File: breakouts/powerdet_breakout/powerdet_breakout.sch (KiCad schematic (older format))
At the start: 22 parts

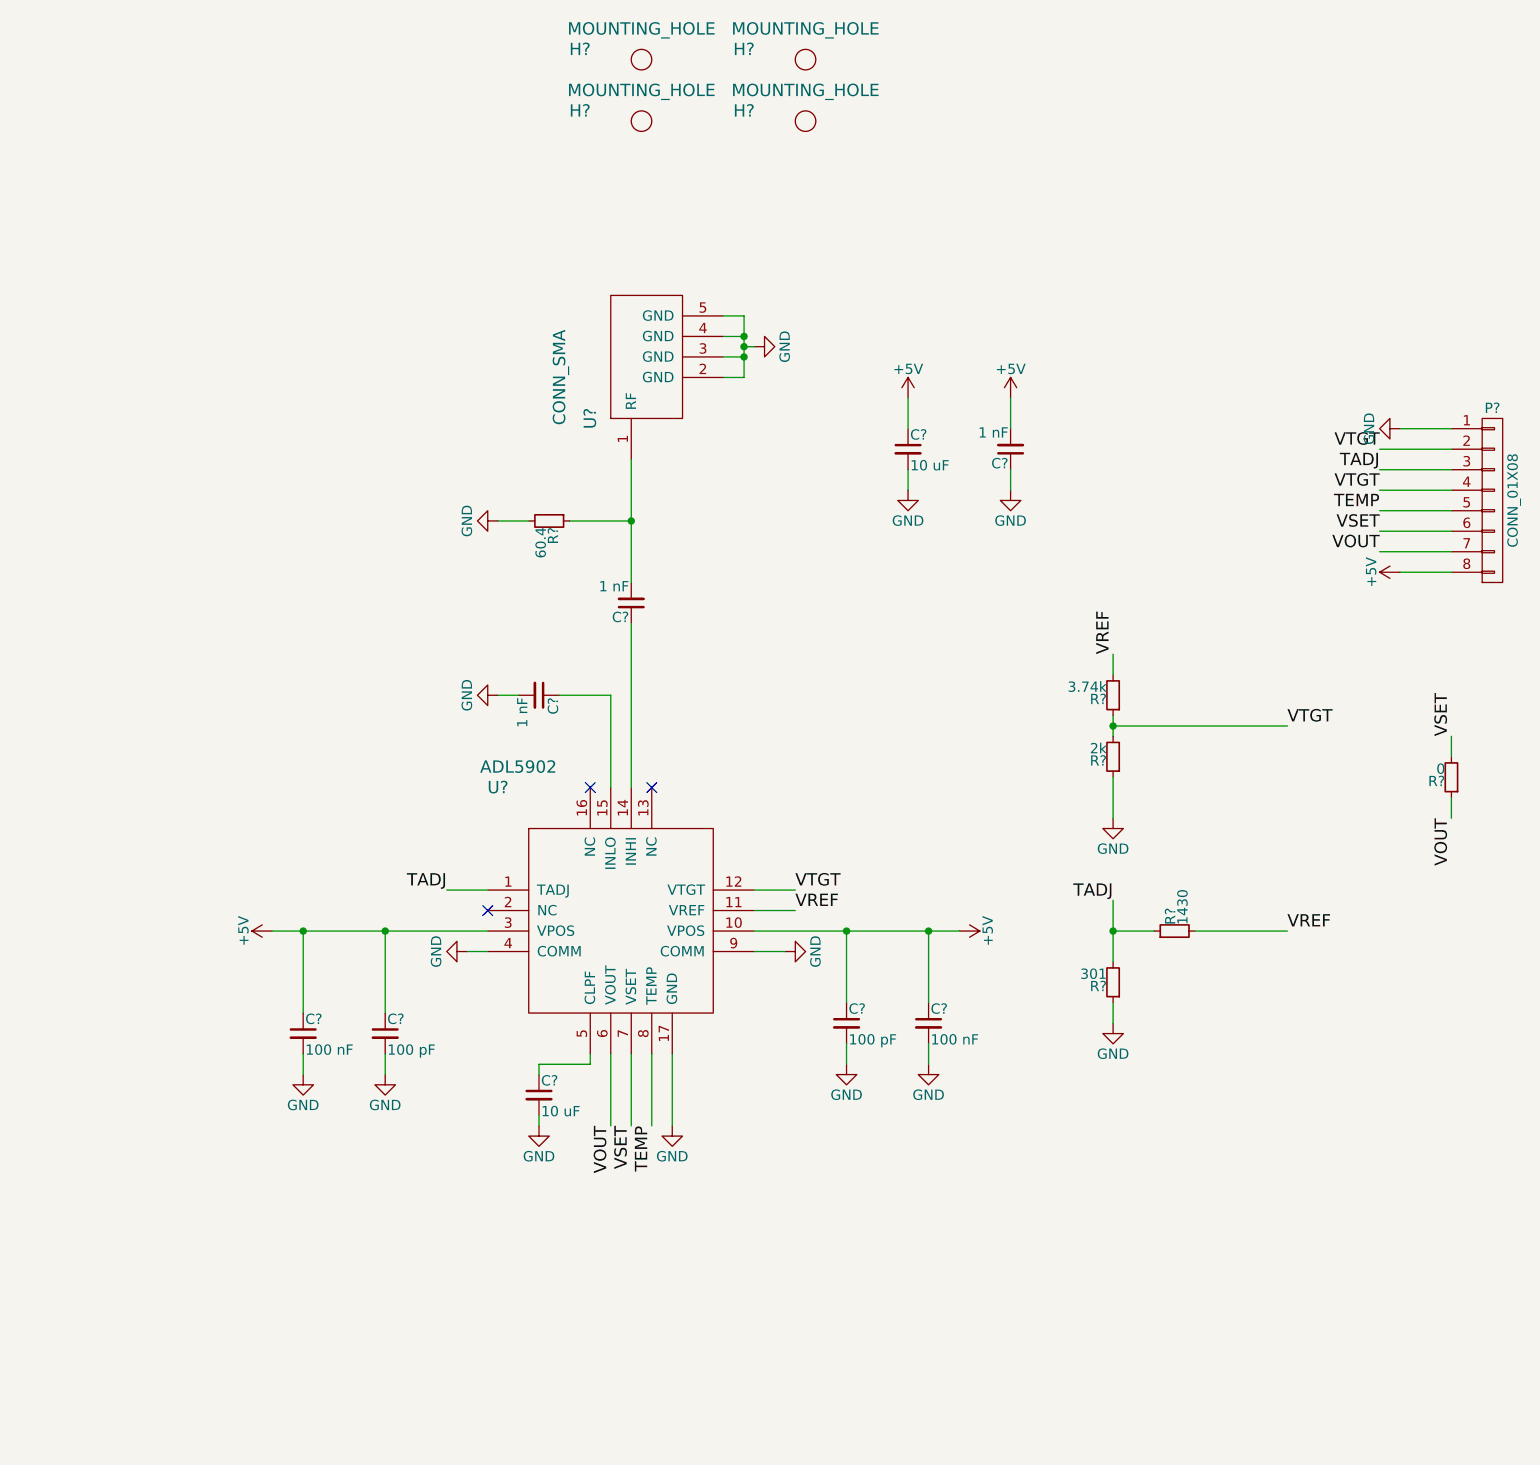
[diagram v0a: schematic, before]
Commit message: started variable attenuator, revised synth, and added power splittert to detect board
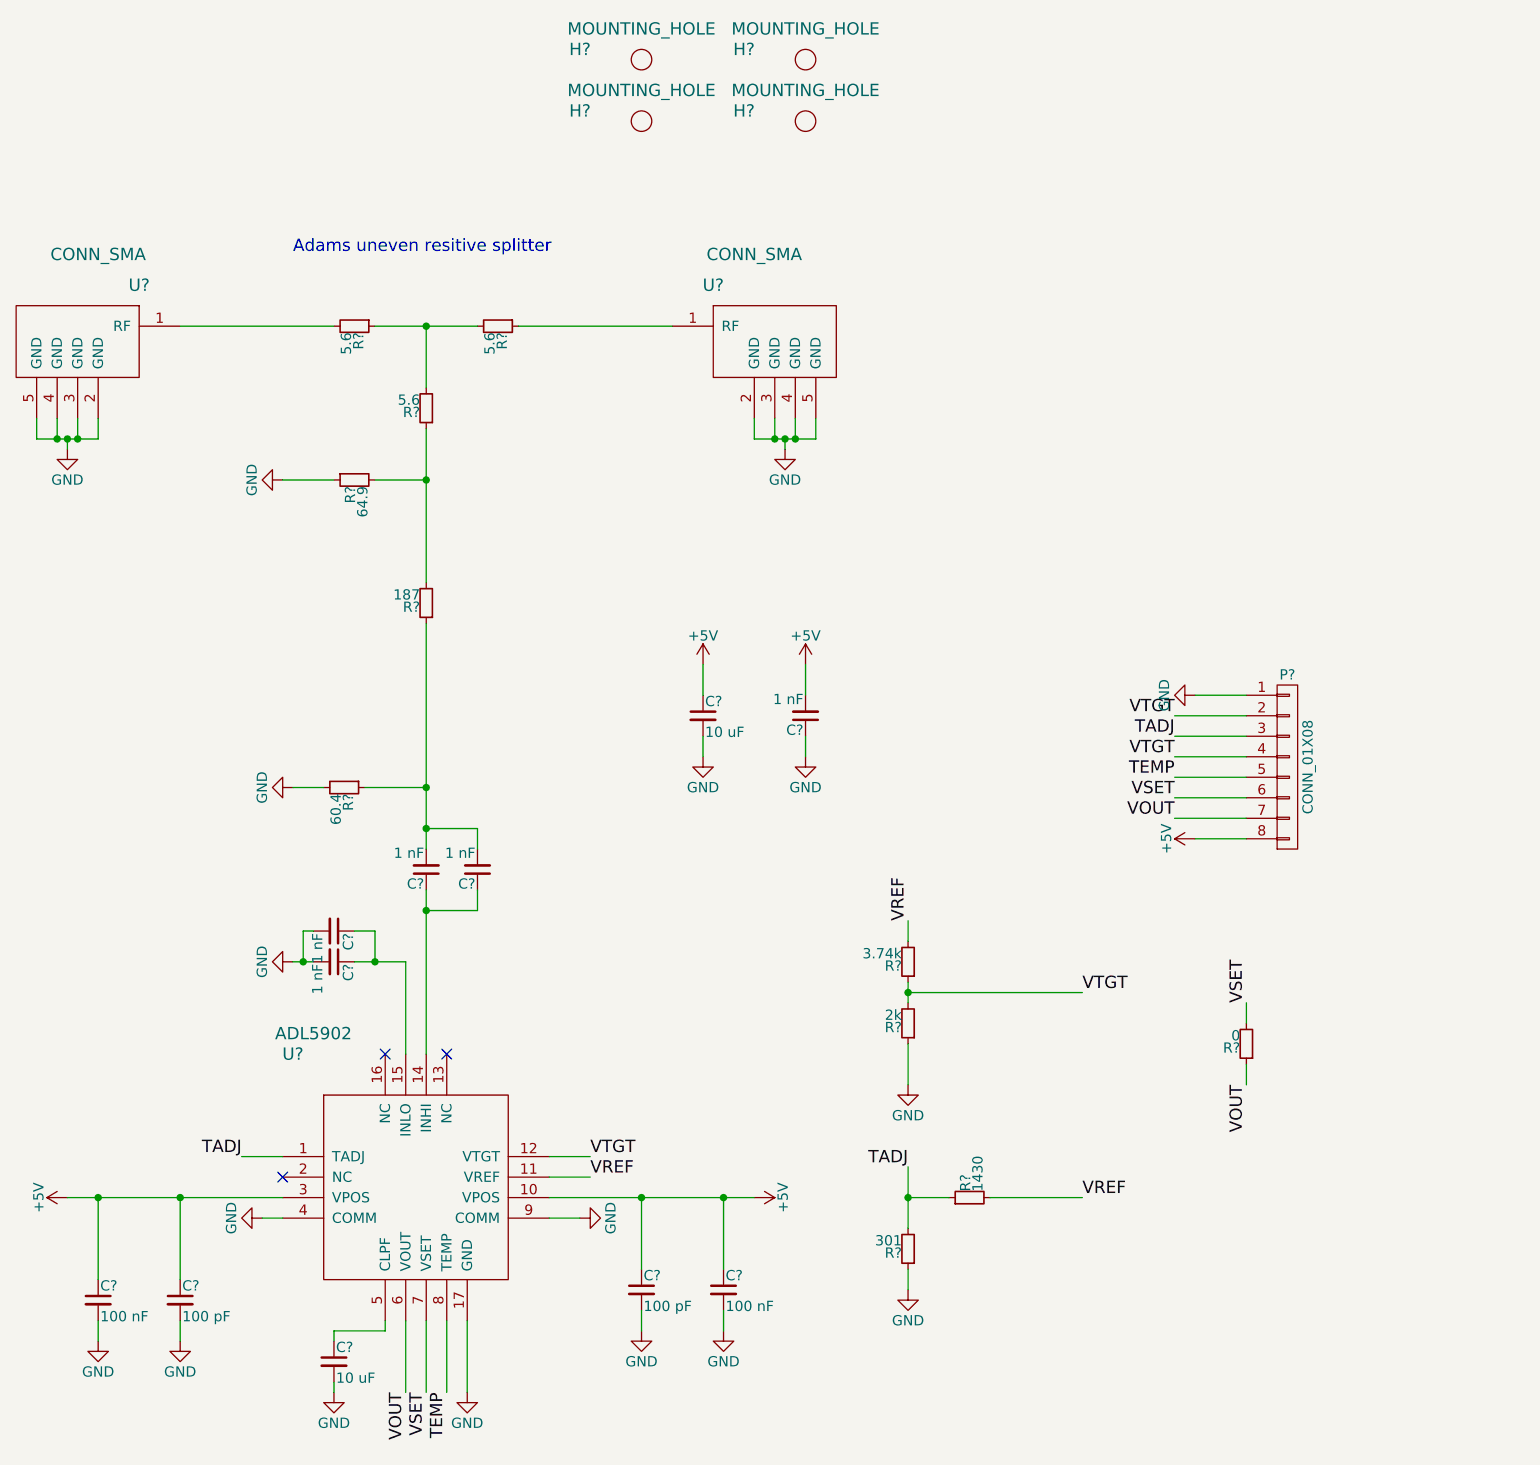
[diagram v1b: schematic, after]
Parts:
- added C? (x2): 1 nF, symbol C_Small
- added R? (x3): 5.6, symbol R_Small
- added R?: 187, symbol R_Small
- added R?: 64.9, symbol R_Small
- added U?: CONN_SMA, symbol CONN_SMA
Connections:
- net GND: now also C?.2, R?.1, U?.2 (GND), U?.3 (GND), U?.4 (GND), U?.5 (GND)
- net at C?.2, R?.1: now also C?.2, R?.1; no longer U?.1 (RF)
- net at C?.1, U?.14 (INHI): now also C?.1
- net at C?.1, U?.15 (INLO): now also C?.1
- new net: R?.2, U?.1 (RF)
- new net: R?.1, U?.1 (RF)
- new net: R?.1, R?.2, R?.2 (x2)
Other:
- note added: "Adams uneven resitive splitter"
- moved on the sheet: C?, P?, R?, U?

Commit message: started and finished variable attenuator layout
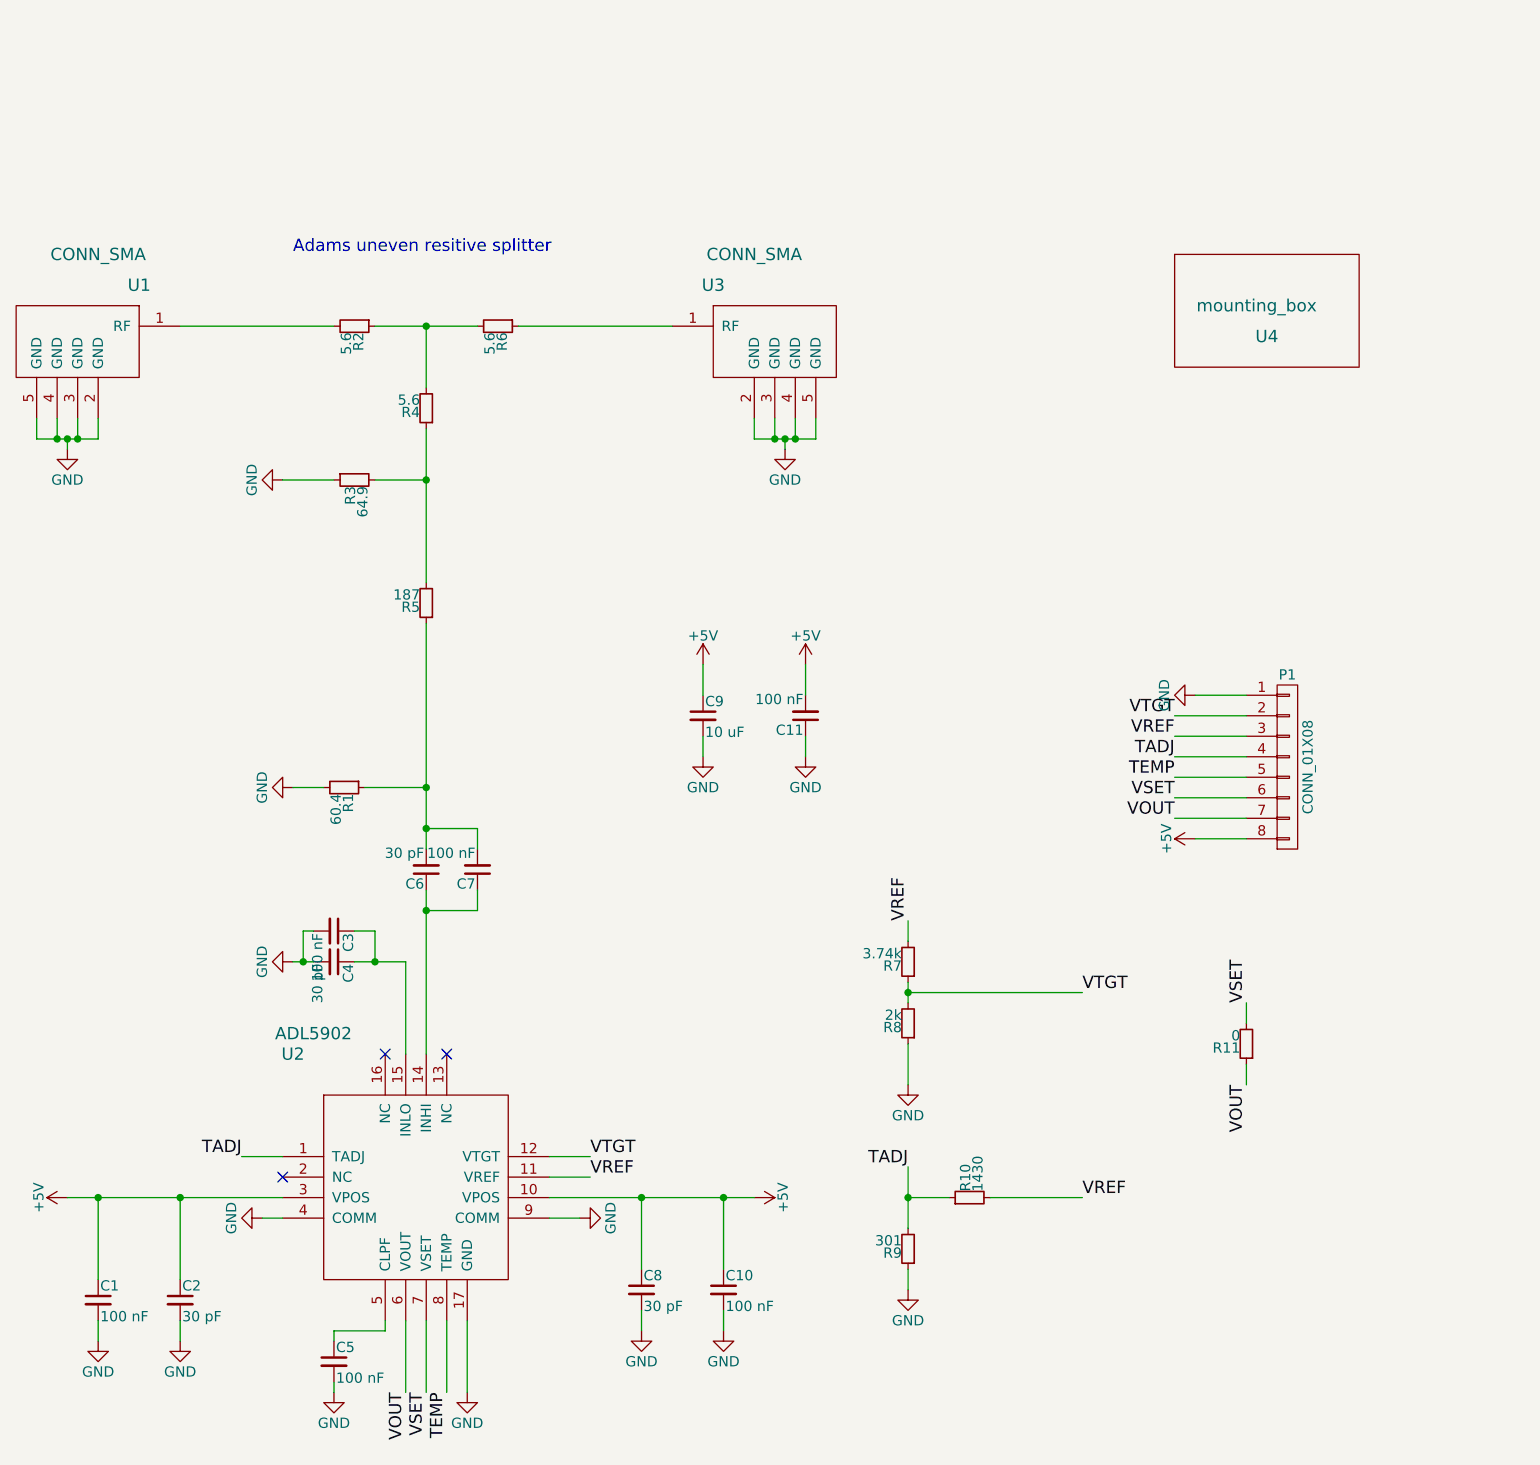
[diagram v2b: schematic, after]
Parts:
- removed H? (x4): MOUNTING_HOLE, symbol MOUNTING_HOLE
- added U4: mounting_box, vna_footprints:POMONA_2400BOX, symbol mounting_box
- C1, C10, C9: renamed from C?; footprint (none) -> Capacitors_SMD:C_0402
- C11, C3, C7: renamed from C?; value 1 nF -> 100 nF; footprint (none) -> Capacitors_SMD:C_0402
- C2, C8: renamed from C?; value 100 pF -> 30 pF; footprint (none) -> Capacitors_SMD:C_0402
- C4, C6: renamed from C?; value 1 nF -> 30 pF; footprint (none) -> Capacitors_SMD:C_0402
- C5: renamed from C?; value 10 uF -> 100 nF; footprint (none) -> Capacitors_SMD:C_0402
- P1: renamed from P?; footprint (none) -> Pin_Headers:Pin_Header_Straight_1x08
- R1, R10, R11, R2, R3, R4, R5, R6, R7, R8, R9: renamed from R?; footprint (none) -> Resistors_SMD:R_0402
- U1, U3: renamed from U?; footprint (none) -> vna_footprints:732512200_SMA
- U2: renamed from U?; footprint (none) -> Housings_DFN_QFN:QFN-16-1EP_4x4mm_Pitch0.65mm
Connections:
- net TADJ: now also P1.4 (P4); no longer P1.3 (P3)
- net VREF: now also P1.3 (P3)
- net VTGT: no longer P1.4 (P4)

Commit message: trimmed ground plane on some breakouts so it doesn't disappear during panelization..
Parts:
- U1, U3: footprint vna_footprints:732512200_SMA -> vna_footprints:732511150_sma
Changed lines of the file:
@@
 F 0 "U1" H 1100 2300 60  0000 C CNN
 F 1 "CONN_SMA" H 1300 2450 60  0000 C CNN
-F 2 "vna_footprints:732512200_SMA" H 1450 2100 60  0001 C CNN
+F 2 "vna_footprints:732511150_sma" H 1450 2100 60  0001 C CNN
 F 3 "" H 1450 2100 60  0000 C CNN
 	1    1450 2100
@@
 F 0 "U3" H 4600 2300 60  0000 C CNN
 F 1 "CONN_SMA" H 4800 2450 60  0000 C CNN
-F 2 "vna_footprints:732512200_SMA" H 4950 2100 60  0001 C CNN
+F 2 "vna_footprints:732511150_sma" H 4950 2100 60  0001 C CNN
 F 3 "" H 4950 2100 60  0000 C CNN
 	1    4950 2100
